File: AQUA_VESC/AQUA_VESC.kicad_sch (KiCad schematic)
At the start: 41 parts, among them J1 Conn_01x06_Pin, J2 Conn_01x02_Pin, U2 SMF05CT1G

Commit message: AQUA VESC仮完成
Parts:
- removed IMU1: WHITE, LED_SMD:LED_0603_1608Metric, symbol Device:LED
- removed R1: 1k, Resistor_SMD:R_0603_1608Metric, symbol Device:R
- removed U1: ~, specific_footprint_library:BMI160_Vertical, symbol specific_library:BMI160_Vertical
- removed UNUSED_GPIO1: Conn_02x04_Odd_Even, Connector_PinSocket_2.54mm:PinSocket_2x04_P2.54mm_Vertical, symbol Connector_Generic:Conn_02x04_Odd_Even
- added NT2: NetTie_2, NetTie:NetTie-2_SMD_Pad2.0mm, symbol Device:NetTie_2
- added NT3: NetTie_2, NetTie:NetTie-2_SMD_Pad0.5mm, symbol Device:NetTie_2
- H5, H6, H7, H8, H9: footprint MountingHole:MountingHole_3.5mm_Pad -> MountingHole:MountingHole_3.5mm_Pad_Via
- SERVO_CNT1: value GREEN -> EMERALD
- USB1: value ~ -> Micro-B
- renumbered R2 to R1, R11 to R10, R12 to R11, R13 to R12, R14 to R13, R3 to R2, R4 to R3, R5 to R4, R6 to R5, R7 to R6, R8 to R7, R9 to R8, R10 to R9, U2 to U1, U3 to U2
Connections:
- net GNDD: now also NT2.1, NT3.1
- net GNDPWR: now also NT2.2, NT3.2
- no-connect marks 5 -> 6
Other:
- sheet STM32F405 ports: added COMM_MOSI, COMM_NSS, MISO_ADC_EXT2; removed ADC_EXT2, MOSI, NSS

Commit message: VESC発注
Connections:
- net GNDPWR: now also RGBLED1.1 (Pin_1); no longer RGBLED1.4 (Pin_4)
- net RGBLED_Driver/BLUE_OUT: now also RGBLED1.2 (Pin_2); no longer RGBLED1.1 (Pin_1)
- net RGBLED_Driver/GREEN_OUT: now also RGBLED1.4 (Pin_4); no longer RGBLED1.3 (Pin_3)
- net RGBLED_Driver/RED_OUT: now also RGBLED1.3 (Pin_3); no longer RGBLED1.2 (Pin_2)
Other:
- moved on the sheet: RGBLED1
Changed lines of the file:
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@@
 	(wire
 		(pts
-			(xy 274.32 179.07) (xy 287.02 179.07)
+			(xy 96.52 175.26) (xy 101.6 175.26)
 		)
 		(stroke
@@
 	(wire
 		(pts
-			(xy 96.52 175.26) (xy 101.6 175.26)
+			(xy 262.89 207.01) (xy 262.89 213.36)
 		)
 		(stroke
@@
 	(wire
 		(pts
-			(xy 262.89 207.01) (xy 262.89 213.36)
+			(xy 260.35 219.71) (xy 262.89 219.71)
 		)
 		(stroke
@@
 	(wire
 		(pts
-			(xy 260.35 219.71) (xy 262.89 219.71)
+			(xy 50.8 154.94) (xy 66.04 154.94)
 		)
 		(stroke
@@
 	(wire
 		(pts
-			(xy 50.8 154.94) (xy 66.04 154.94)
+			(xy 284.48 176.53) (xy 287.02 176.53)
 		)
 		(stroke
@@
 	(wire
 		(pts
-			(xy 274.32 181.61) (xy 287.02 181.61)
-		)
-		(stroke
-			(width 0)
-			(type default)
-		)
-	)
-	(wire
-		(pts
 			(xy 115.57 96.52) (xy 124.46 96.52)
 		)
@@
 	(wire
 		(pts
-			(xy 284.48 186.69) (xy 287.02 186.69)
-		)
-		(stroke
-			(width 0)
-			(type default)
-		)
-	)
-	(wire
-		(pts
 			(xy 208.28 119.38) (xy 242.57 119.38)
 		)
@@
 	(wire
 		(pts
-			(xy 274.32 184.15) (xy 287.02 184.15)
-		)
-		(stroke
-			(width 0)
-			(type default)
-		)
-	)
-	(wire
-		(pts
 			(xy 124.46 138.43) (xy 124.46 142.24)
 		)
@@
 	(wire
 		(pts
+			(xy 274.32 181.61) (xy 287.02 181.61)
+		)
+		(stroke
+			(width 0)
+			(type default)
+		)
+	)
+	(wire
+		(pts
 			(xy 274.32 129.54) (xy 311.15 129.54)
 		)
@@
 	(wire
 		(pts
+			(xy 274.32 179.07) (xy 287.02 179.07)
+		)
+		(stroke
+			(width 0)
+			(type default)
+		)
+	)
+	(wire
+		(pts
+			(xy 274.32 184.15) (xy 287.02 184.15)
+		)
+		(stroke
+			(width 0)
+			(type default)
+		)
+	)
+	(wire
+		(pts
 			(xy 231.14 195.58) (xy 231.14 198.12)
 		)
@@
 	(wire
 		(pts
-			(xy 284.48 191.77) (xy 284.48 186.69)
-		)
-		(stroke
-			(width 0)
-			(type default)
-		)
-	)
-	(wire
-		(pts
 			(xy 114.3 93.98) (xy 124.46 93.98)
 		)
@@
 	(symbol
 		(lib_id "Connector:Conn_01x04_Pin")
-		(at 292.1 181.61 0)
+		(at 292.1 179.07 0)
 		(mirror y)
 		(unit 1)
@@
 		(dnp no)
 		(property "Reference" "RGBLED1"
-			(at 297.18 178.816 0)
+			(at 297.18 176.276 0)
 			(effects
 				(font
@@
 		)
 		(property "Value" "Conn_01x04_Pin"
-			(at 295.91 175.514 0)
+			(at 295.91 172.974 0)
 			(effects
 				(font
@@
 		)
 		(property "Footprint" "Connector_JST:JST_XA_S04B-XASK-1N-BN_1x04_P2.50mm_Horizontal"
-			(at 292.1 181.61 0)
+			(at 292.1 179.07 0)
 			(effects
 				(font
@@
 		)
 		(property "Datasheet" "~"
-			(at 292.1 181.61 0)
+			(at 292.1 179.07 0)
 			(effects
 				(font
@@
 		)
 		(property "Description" "Generic connector, single row, 01x04, script generated"
-			(at 292.1 181.61 0)
+			(at 292.1 179.07 0)
 			(effects
 				(font
@@
 	(symbol
 		(lib_id "power:GNDPWR")
-		(at 284.48 191.77 0)
+		(at 284.48 176.53 0)
 		(unit 1)
 		(exclude_from_sim no)
@@
 		(fields_autoplaced yes)
 		(property "Reference" "#PWR022"
-			(at 284.48 196.85 0)
+			(at 284.48 181.61 0)
 			(effects
 				(font
@@
 		)
 		(property "Value" "GNDPWR"
-			(at 284.353 195.58 0)
+			(at 284.353 180.34 0)
 			(effects
 				(font
@@
 		)
 		(property "Footprint" ""
-			(at 284.48 193.04 0)
+			(at 284.48 177.8 0)
 			(effects
 				(font
@@
 		)
 		(property "Datasheet" ""
-			(at 284.48 193.04 0)
+			(at 284.48 177.8 0)
 			(effects
 				(font
@@
 		)
 		(property "Description" "Power symbol creates a global label with name \"GNDPWR\" , global ground"
-			(at 284.48 191.77 0)
+			(at 284.48 176.53 0)
 			(effects
 				(font

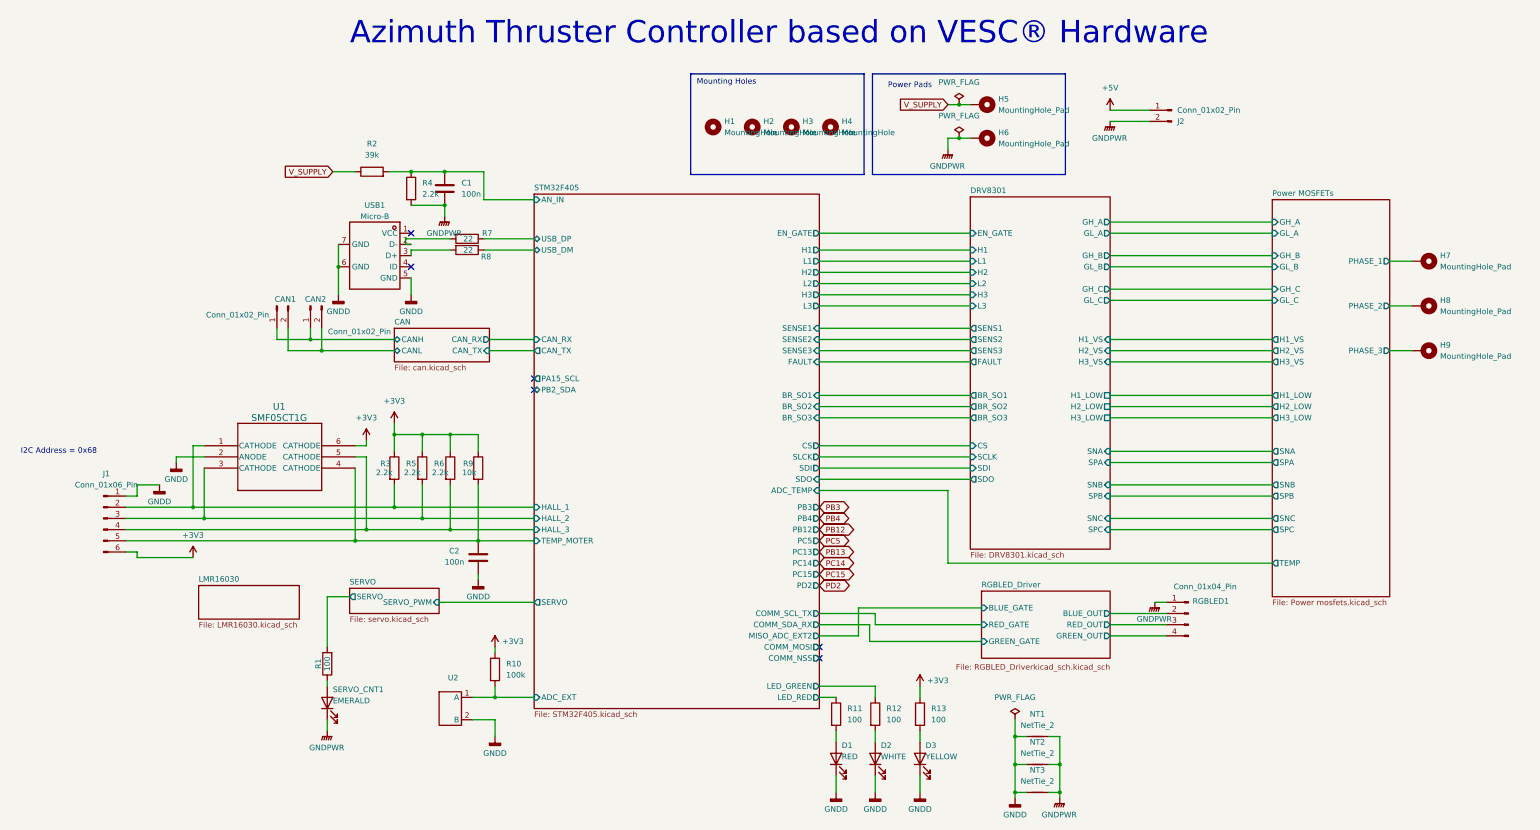
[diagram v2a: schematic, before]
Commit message: AQUA_VESC REV01作成
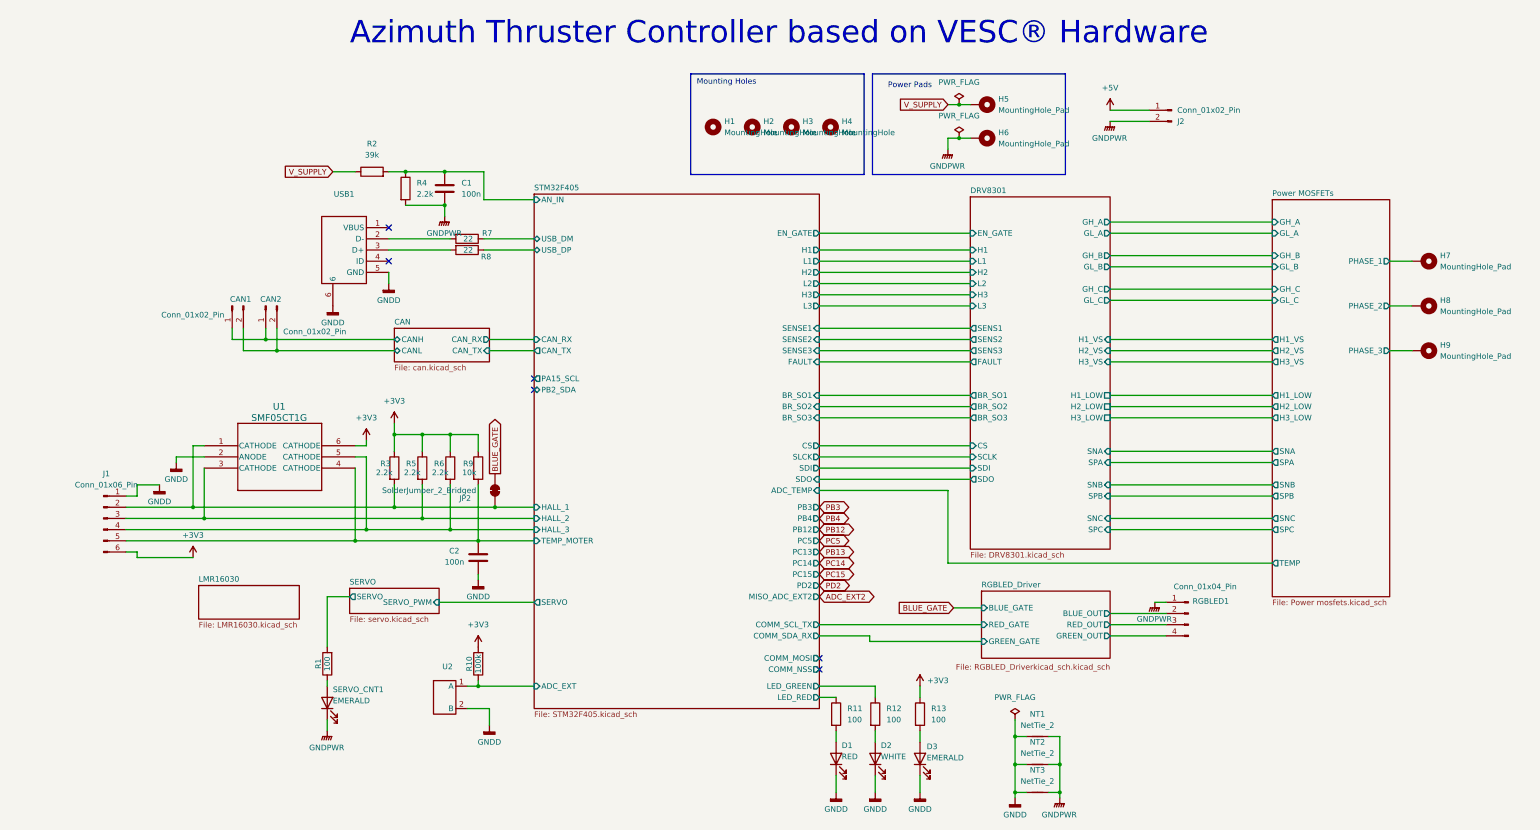
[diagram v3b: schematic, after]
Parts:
- removed USB1: Micro-B, specific_footprint_library:MICRO-USB-SMD_MICRO-QTZB5.5, symbol specific_library:MICRO QTZB5.5
- added JP2: SolderJumper_2_Bridged, Jumper:SolderJumper-2_P1.3mm_Bridged_RoundedPad1.0x1.5mm, symbol Jumper:SolderJumper_2_Bridged
- added USB1: ~, specific_footprint_library:MICRO-USB-SMD_5P-P0.65-H-F_MICRO5.9MMUSB, symbol specific_library:MICRO5.9MMUSB
- CAN1, CAN2: footprint Connector_JST:JST_XA_S02B-XASK-1N-BN_1x02_P2.50mm_Horizontal -> Connector_JST:JST_XA_S02B-XASK-1_1x02_P2.50mm_Horizontal
- D3: value YELLOW -> EMERALD
- J1: footprint Connector_JST:JST_XA_S06B-XASK-1N-BN_1x06_P2.50mm_Horizontal -> Connector_JST:JST_XA_S06B-XASK-1_1x06_P2.50mm_Horizontal
- R10: footprint Resistor_SMD:R_0603_1608Metric_Pad0.98x0.95mm_HandSolder -> Resistor_SMD:R_0603_1608Metric
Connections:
- net +3V3: now also R10.2; no longer R10.1
- net GNDD: now also USB1.5 (GND), USB1.6
- net STM32F405/ADC_EXT: now also R10.1; no longer R10.2
- net STM32F405/HALL_1: now also JP2.1 (A)
- net STM32F405/USB_DM: now also R7.1; no longer R8.1
- net STM32F405/USB_DP: now also R8.1; no longer R7.1
- net at R7.2: now also USB1.2 (D-)
- net at R8.2: now also USB1.3 (D+)
- new net BLUE_GATE: JP2.2 (B)
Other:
- note removed: "I2C Address = 0x68"
- moved on the sheet: CAN1, CAN2, R4, U2

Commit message: 制御基板REV01完成
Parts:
- removed CAN1, CAN2: Conn_01x02_Pin, Connector_JST:JST_XA_S02B-XASK-1_1x02_P2.50mm_Horizontal, symbol Connector:Conn_01x02_Pin
- removed J1: Conn_01x06_Pin, Connector_JST:JST_XA_S06B-XASK-1_1x06_P2.50mm_Horizontal, symbol Connector:Conn_01x06_Pin
- removed J2: Conn_01x02_Pin, Connector_PinHeader_2.54mm:PinHeader_1x02_P2.54mm_Vertical, symbol Connector:Conn_01x02_Pin
- removed R1: 100, Resistor_SMD:R_0603_1608Metric, symbol Device:R
- removed SERVO_CNT1: EMERALD, LED_SMD:LED_0805_2012Metric, symbol Device:LED
- added J1: Conn_01x12_Socket, Connector_PinSocket_2.54mm:PinSocket_1x12_P2.54mm_Horizontal, symbol Connector:Conn_01x12_Socket
- RGBLED1: footprint Connector_JST:JST_XA_S04B-XASK-1N-BN_1x04_P2.50mm_Horizontal -> Connector_PinSocket_2.54mm:PinSocket_1x04_P2.54mm_Horizontal
- renumbered JP2 to JP1, R2 to R1, R11 to R10, R12 to R11, R13 to R12, R3 to R2, R4 to R3, R5 to R4, R6 to R5, R7 to R6, R8 to R7, R9 to R8, R10 to R9
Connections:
- net +3V3: now also J1.12 (Pin_12)
- net +5V: now also J1.1 (Pin_1)
- net CAN/CANH: now also J1.2 (Pin_2), J1.5 (Pin_5)
- net CAN/CANL: now also J1.3 (Pin_3), J1.6 (Pin_6)
- net GNDD: now also J1.4 (Pin_4), J1.7 (Pin_7)
- net STM32F405/HALL_1: now also J1.8 (Pin_8)
- net STM32F405/HALL_2: now also J1.9 (Pin_9)
- net STM32F405/HALL_3: now also J1.10 (Pin_10)
- net STM32F405/TEMP_MOTER: now also J1.11 (Pin_11)
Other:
- removed sheet LMR16030
- added sheet LM76002 (LM76002.kicad_sch)
- sheet SERVO ports: added none; removed SERVO

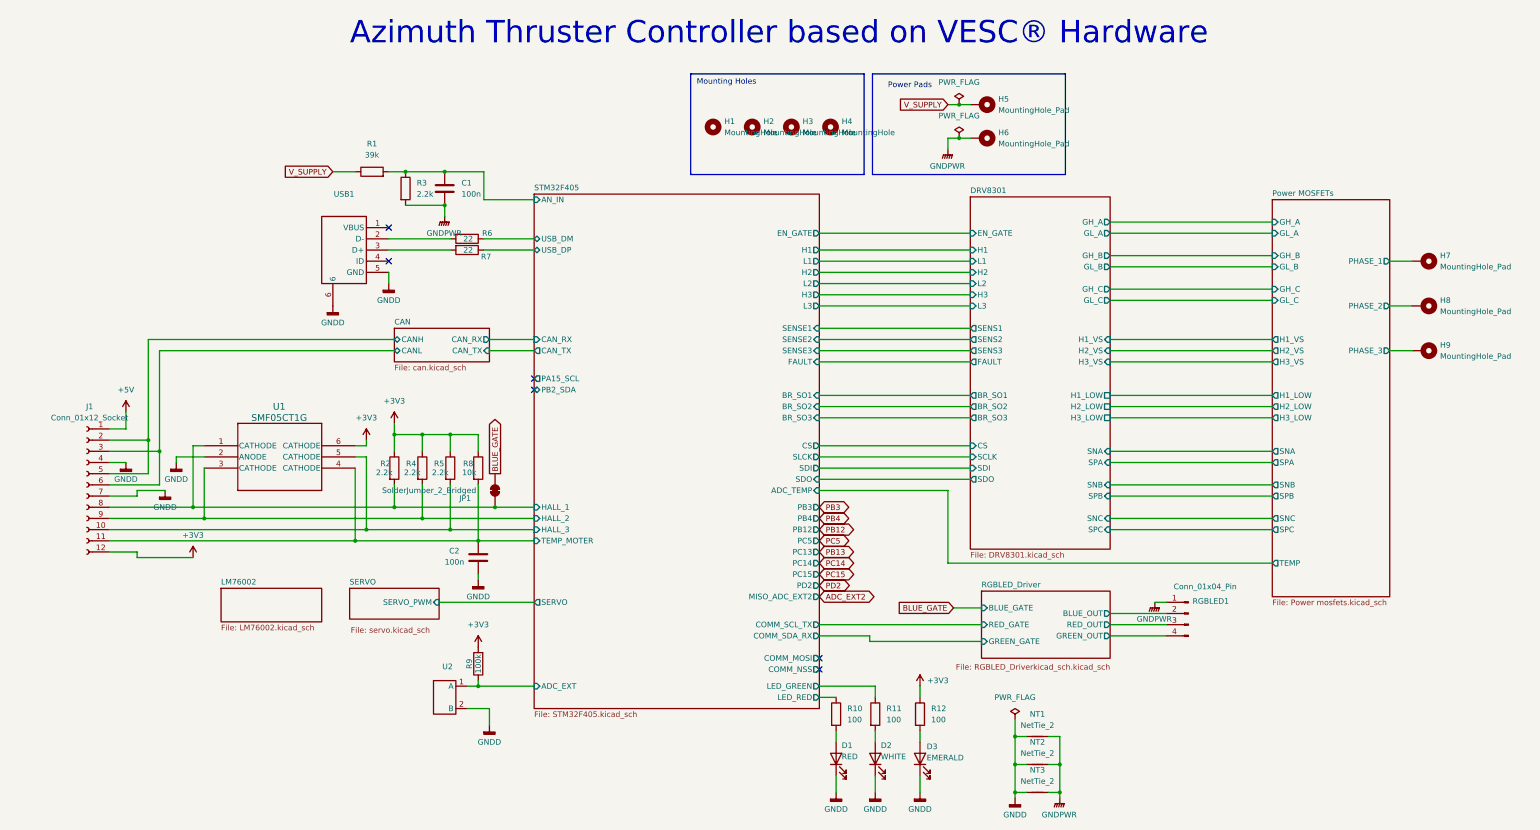
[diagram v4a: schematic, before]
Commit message: 方針変更、back_connector_escにMT60を使用しないことに
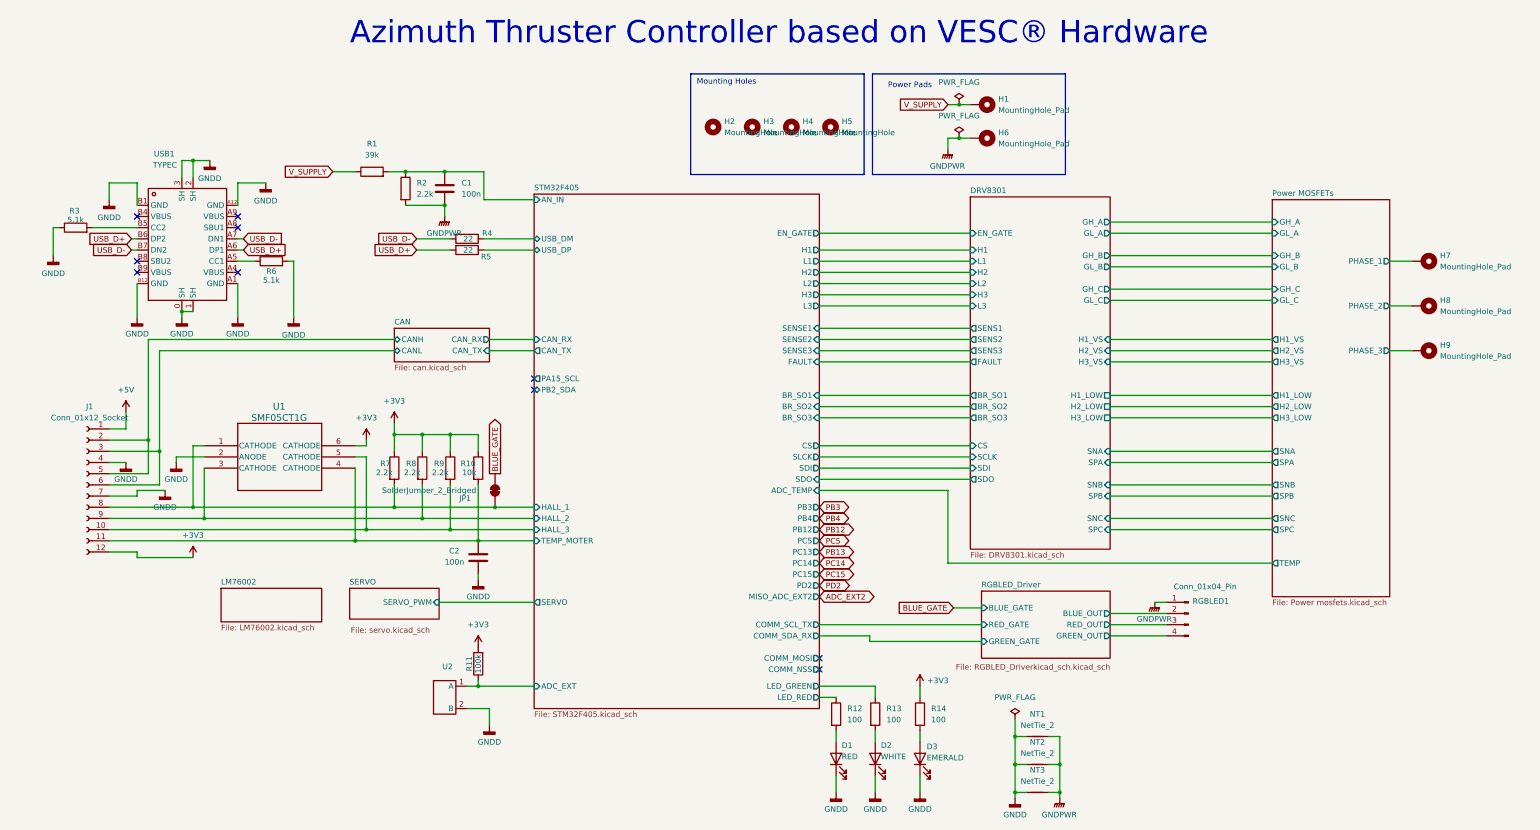
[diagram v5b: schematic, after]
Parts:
- removed USB1: ~, specific_footprint_library:MICRO-USB-SMD_5P-P0.65-H-F_MICRO5.9MMUSB, symbol specific_library:MICRO5.9MMUSB
- added R3, R6: 5.1k, Resistor_SMD:R_0603_1608Metric, symbol Device:R
- added USB1: TYPEC, specific_footprint_library:USB-C_SMD-TYPE-C-31-M-12, symbol specific_library:USB-TYPE-C-018
- renumbered H5 to H1, H1 to H2, H2 to H3, H3 to H4, H4 to H5, R8 to R10, R9 to R11, R10 to R12, R11 to R13, R12 to R14, R3 to R2, R6 to R4, R7 to R5, R2 to R7, R4 to R8, R5 to R9
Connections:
- net GNDD: now also R3.1, R6.2, USB1.0 (SH), USB1.1 (SH), USB1.2 (SH), USB1.3 (SH), USB1.A1 (GND), USB1.A12 (GND), USB1.B1 (GND), USB1.B12 (GND)
- net USB_D-: now reaches R4.2
- net USB_D-: now also USB1.A7 (DN1), USB1.B7 (DN2)
- net USB_D+: now reaches R5.2
- net USB_D+: now also USB1.A6 (DP1), USB1.B6 (DP2)
- new net: R3.2, USB1.B5 (CC2)
- new net: R6.1, USB1.A5 (CC1)
- no-connect marks 6 -> 10

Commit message: ESC周りの配線用基板進捗
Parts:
- U2: footprint basic_parts:wetness sensor -> specific_footprint_library:wetness sensor
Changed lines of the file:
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@@
 			)
 		)
-		(property "Footprint" "basic_parts:wetness sensor"
+		(property "Footprint" "specific_footprint_library:wetness sensor"
 			(at 123.19 199.39 0)
 			(effects
